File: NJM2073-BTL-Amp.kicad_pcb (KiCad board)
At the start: 2 copper layers, 133.4 x 80.6 mm, 84 parts, among them J1 Screw_Terminal_01x02, J2 Screw_Terminal_01x02, J3 Barrel_Jack_Switch, J4 Conn_Coaxial_x2, J5 AudioJack3_SwitchTR, U1 NJM2073, U2 NJM2073, U3 NJM4558, U4 NJM4558, U5 LM317_TO-220

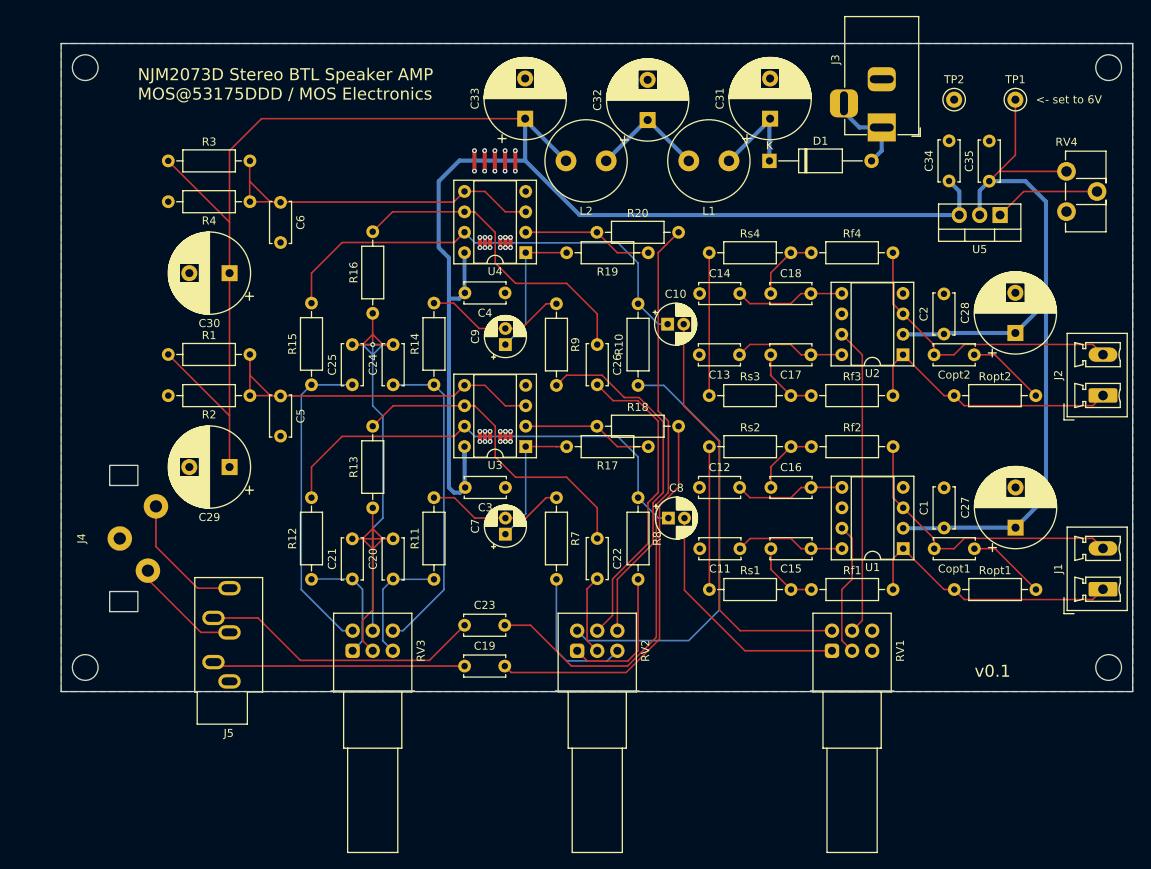
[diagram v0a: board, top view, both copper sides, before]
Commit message: 配線修正
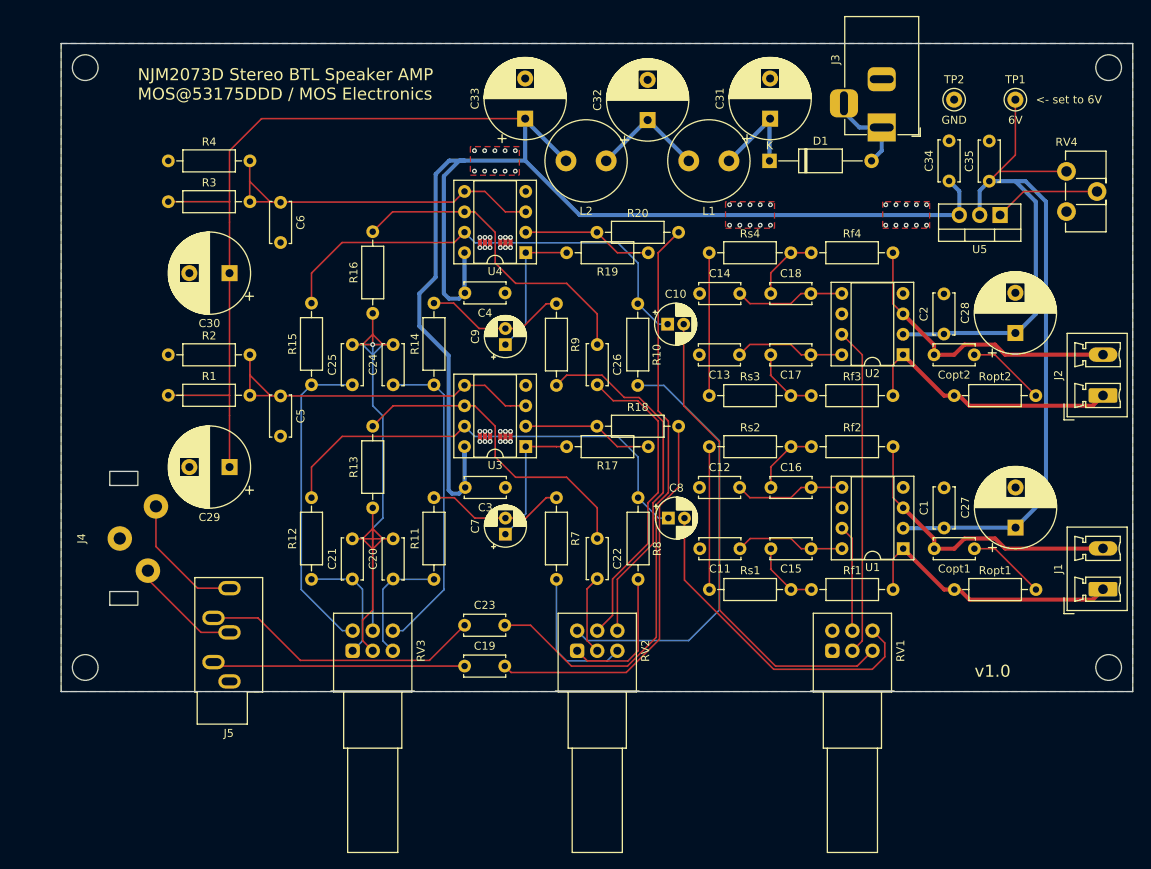
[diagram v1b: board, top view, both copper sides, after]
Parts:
- moved R2 11.4 mm to (125.7, 91.4), turned to 0 degrees
- moved R4 11.4 mm to (125.7, 67.3), turned to 0 degrees
- moved R10 10.2 mm to (184.2, 85.1), turned to -90 degrees
- moved R1 5.08 mm to (125.7, 96.5)
- moved R3 5.08 mm to (125.7, 72.4)
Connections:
- R10 pad 1: Net-(R10-Pad1) -> Net-(C10-Pad1)
- R10 pad 2: Net-(C10-Pad1) -> Net-(R10-Pad2)
- R2 pad 1: Net-(U3A-+) -> GND
- R2 pad 2: GND -> Net-(U3A-+)
- R4 pad 1: Net-(U4A-+) -> GND
- R4 pad 2: GND -> Net-(U4A-+)
- RV1 pad 1: Filtered-signal-L -> GND
- RV1 pad 2: Net-(U1A-AIN+) -> Net-(U2A-AIN+)
- RV1 pad 3: GND -> Filtered-signal-R
- RV1 pad 4: Filtered-signal-R -> GND
- RV1 pad 5: Net-(U2A-AIN+) -> Net-(U1A-AIN+)
- RV1 pad 6: GND -> Filtered-signal-L
- RV2 pad 4: Net-(R10-Pad1) -> Net-(R10-Pad2)
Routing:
- net Net-(R10-Pad2): track 0.00 -> 53.8 mm
- net Net-(R10-Pad1): track 53.8 -> 0.00 mm
- net +6V: track 108.2 -> 124.0 mm
- net +12V: track 240.3 -> 255.9 mm
- net GND: track 27.9 -> 15.2 mm, vias 34 -> 54
- net Filtered-signal-L: track 30.5 -> 41.8 mm
- net Filtered-signal-R: track 52.5 -> 60.1 mm
- net Net-(U1A-AIN+): track 16.8 -> 13.3 mm
- net Net-(U2A-AIN+): track 38.5 -> 40.9 mm
- added copper zone on F.Cu, net GND
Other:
- board text added: "${REFERENCE}"
- board text added: "6V"
- board text added: "GND"
- board text added: "v1.0"
- board text removed: "v0.1"

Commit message: ちょいと修正
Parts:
- C27, C28, C29, C30, C31, C32, C33: footprint Capacitor_THT:CP_Radial_D10.0mm_P5.00mm -> Capacitor_THT:CP_Radial_D6.3mm_P2.50mm
- moved J4 33.5 mm to (112.3, 80.8)
- moved J5 24.6 mm to (114.3, 116.6), turned to 90 degrees
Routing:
- net Input_L: track 31.5 -> 59.1 mm
- net /L: track 16.3 -> 42.2 mm
- net Input_R: track 35.3 -> 55.0 mm
- net /R: track 14.0 -> 32.9 mm
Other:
- board text added: "Lch-OUT"
- board text added: "Rch-OUT"
